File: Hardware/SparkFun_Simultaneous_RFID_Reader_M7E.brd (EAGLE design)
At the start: 35.6 x 61 mm, 76 parts, among them J5 U.FL, U1 UHF_RFID_NANO_MODULE_M7E_HECTO, U2 CH340C

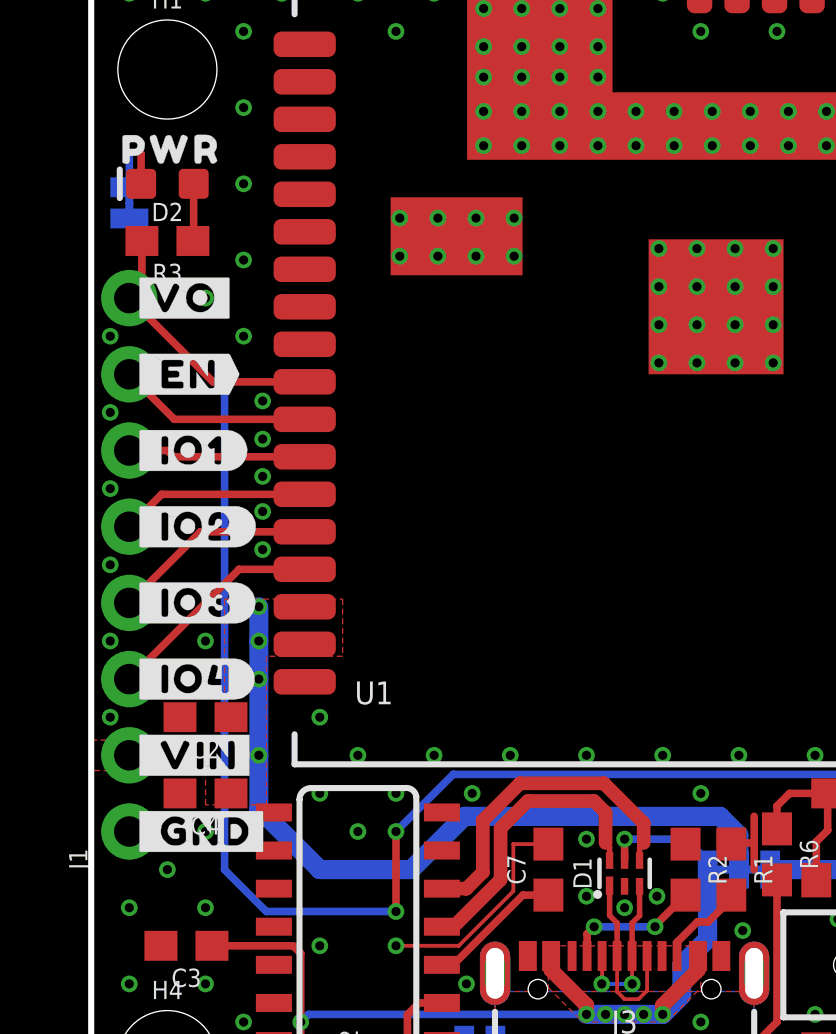
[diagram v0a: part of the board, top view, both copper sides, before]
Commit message: Design review updates
Add polygons to better fan out USB traces from ESD diode pads
Nudge R3 away from VOUT pad
Add VOUT range to schematic
Swap power LED and resistor for new version
Move via out of VO silk label
Nudge USB traces to get better GND pour around C7
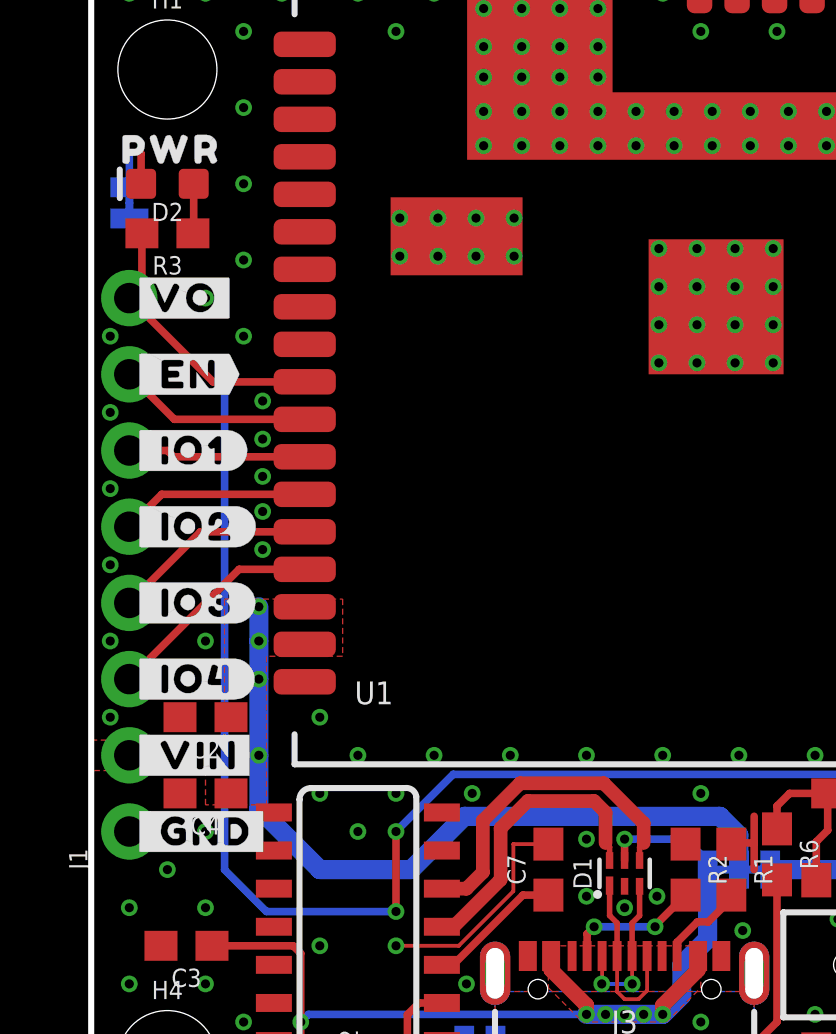
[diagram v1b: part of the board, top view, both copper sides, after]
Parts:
- moved R3 0.25 mm to (2.54, 30.1)
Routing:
- added copper zone on layer 1, net USB_N
- added copper zone on layer 1, net USB_P
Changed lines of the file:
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@@
 <drawing>
 <settings>
-<setting alwaysvectorfont="yes"/>
+<setting alwaysvectorfont="no"/>
 <setting verticaltext="up"/>
 </settings>
@@
 <attribute name="VALUE" x="0.127" y="31.115" size="0.6096" layer="28" font="vector" ratio="20" rot="MR90" align="top-center"/>
 </element>
-<element name="R3" library="SparkFun-Resistors" package="0603" value="1k" x="2.54" y="29.845" smashed="yes" rot="R180">
-<attribute name="NAME" x="2.54" y="29.083" size="0.6096" layer="25" font="vector" ratio="20" rot="R180" align="bottom-center"/>
-<attribute name="PROD_ID" value="RES-07856" x="2.54" y="29.845" size="1.778" layer="27" font="vector" ratio="15" rot="R180" display="off"/>
-<attribute name="VALUE" x="2.54" y="30.607" size="0.6096" layer="27" font="vector" ratio="20" rot="R180" align="top-center"/>
+<element name="R3" library="SparkFun-Resistors" package="0603" value="1k" x="2.54" y="30.099" smashed="yes" rot="R180">
+<attribute name="NAME" x="2.54" y="29.337" size="0.6096" layer="25" font="vector" ratio="20" rot="R180" align="bottom-center"/>
+<attribute name="PROD_ID" value="RES-07856" x="2.54" y="30.099" size="1.778" layer="27" font="vector" ratio="15" rot="R180" display="off"/>
+<attribute name="VALUE" x="2.54" y="30.861" size="0.6096" layer="27" font="vector" ratio="20" rot="R180" align="top-center"/>
 </element>
 <element name="U$49" library="output" package="#PWR#0" value="" x="1.905" y="31.115" smashed="yes" rot="MR0"/>
@@
 <wire x1="17.145" y1="10.795" x2="16.764" y2="11.176" width="0.4572" layer="1"/>
 <wire x1="16.764" y1="11.176" x2="14.5542" y2="11.176" width="0.4572" layer="1"/>
+<polygon width="0.18541875" layer="1" isolate="0.127" thermals="no">
+<vertex x="17.2974" y="9.4234"/>
+<vertex x="17.2974" y="9.906"/>
+<vertex x="17.018" y="9.906"/>
+<vertex x="17.018" y="9.7028"/>
+</polygon>
 </signal>
 <signal name="USB_N" class="1">
@@
 <wire x1="18.415" y1="10.4394" x2="17.08658125" y2="11.76781875" width="0.4572" layer="1"/>
 <wire x1="17.08658125" y1="11.76781875" x2="14.29778125" y2="11.76781875" width="0.4572" layer="1"/>
+<polygon width="0.18541875" layer="1" isolate="0.127" thermals="no">
+<vertex x="18.2626" y="9.4234"/>
+<vertex x="18.2626" y="9.906"/>
+<vertex x="18.542" y="9.906"/>
+<vertex x="18.542" y="9.7028"/>
+</polygon>
 </signal>
 <signal name="V_USB">
@@
 <contactref element="R3" pad="1"/>
 <contactref element="D2" pad="A"/>
-<wire x1="3.39" y1="29.845" x2="3.417" y2="29.872" width="0.254" layer="1"/>
-<wire x1="3.417" y1="29.872" x2="3.417" y2="31.75" width="0.254" layer="1"/>
+<wire x1="3.39" y1="30.099" x2="3.417" y2="30.126" width="0.254" layer="1"/>
+<wire x1="3.417" y1="30.126" x2="3.417" y2="31.75" width="0.254" layer="1"/>
 </signal>
 <signal name="N$6">
@@
 <wire x1="29.21" y1="10.16" x2="28.575" y2="10.795" width="0.254" layer="16"/>
 <contactref element="R3" pad="2"/>
-<wire x1="1.69" y1="28.36" x2="1.69" y2="29.845" width="0.254" layer="1"/>
+<wire x1="1.69" y1="28.36" x2="1.69" y2="30.099" width="0.254" layer="1"/>
 <wire x1="1.27" y1="27.94" x2="1.69" y2="28.36" width="0.254" layer="1"/>
 </signal>

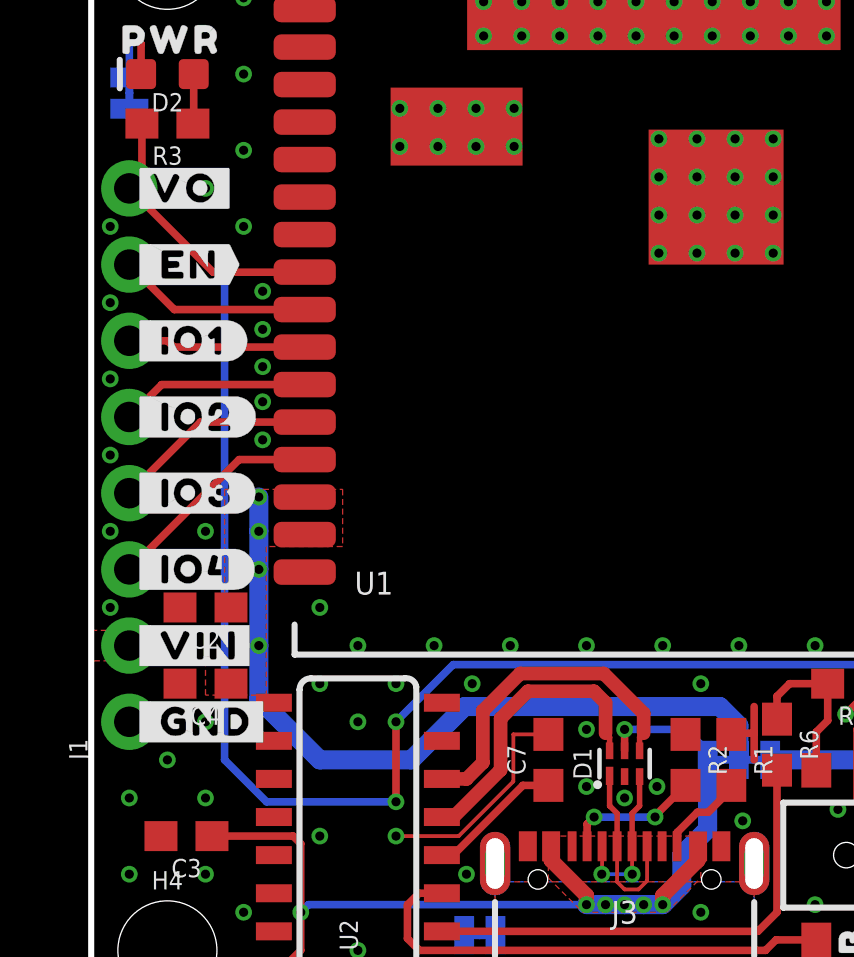
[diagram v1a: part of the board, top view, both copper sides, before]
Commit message: Design review update
Actually update the power LED and resistor this time
Actually move the via on the VO silk this time
Actually nudge USB traces to get better GND pour around C7 this time
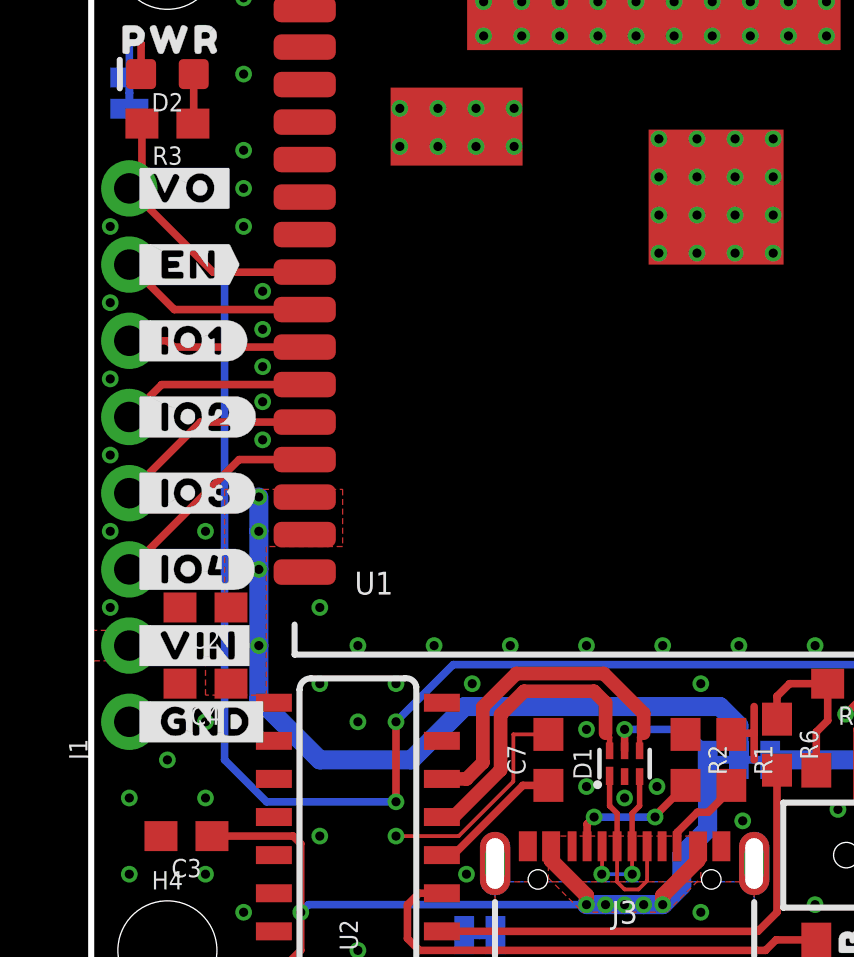
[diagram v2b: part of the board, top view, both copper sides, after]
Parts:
- R3: value 1k -> 4.7k
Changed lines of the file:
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@@
 <element name="D2" library="SparkFun-LED" package="LED-0603" value="Red" x="2.54" y="31.75" smashed="yes" rot="R180">
 <attribute name="NAME" x="2.54" y="31.115" size="0.6096" layer="25" font="vector" ratio="20" rot="R180" align="bottom-center"/>
-<attribute name="PROD_ID" value="DIO-00819" x="2.54" y="31.75" size="1.778" layer="27" font="vector" ratio="15" rot="R180" display="off"/>
+<attribute name="PROD_ID" value="DIO-17976" x="2.54" y="31.75" size="1.778" layer="27" font="vector" ratio="15" rot="R180" display="off"/>
 <attribute name="VALUE" value="Red" x="2.54" y="32.385" size="0.6096" layer="27" font="vector" ratio="20" rot="R180" align="top-center"/>
 </element>
@@
 <attribute name="VALUE" x="0.127" y="31.115" size="0.6096" layer="28" font="vector" ratio="20" rot="MR90" align="top-center"/>
 </element>
-<element name="R3" library="SparkFun-Resistors" package="0603" value="1k" x="2.54" y="30.099" smashed="yes" rot="R180">
+<element name="R3" library="SparkFun-Resistors" package="0603" value="4.7k" x="2.54" y="30.099" smashed="yes" rot="R180">
 <attribute name="NAME" x="2.54" y="29.337" size="0.6096" layer="25" font="vector" ratio="20" rot="R180" align="bottom-center"/>
-<attribute name="PROD_ID" value="RES-07856" x="2.54" y="30.099" size="1.778" layer="27" font="vector" ratio="15" rot="R180" display="off"/>
-<attribute name="VALUE" x="2.54" y="30.861" size="0.6096" layer="27" font="vector" ratio="20" rot="R180" align="top-center"/>
+<attribute name="PROD_ID" value="RES-07857" x="2.54" y="30.099" size="1.778" layer="27" font="vector" ratio="15" rot="R180" display="off"/>
+<attribute name="VALUE" value="4.7k" x="2.54" y="30.861" size="0.6096" layer="27" font="vector" ratio="20" rot="R180" align="top-center"/>
 </element>
 <element name="U$49" library="output" package="#PWR#0" value="" x="1.905" y="31.115" smashed="yes" rot="MR0"/>
@@
 <via x="5.08" y="36.83" extent="1-16" drill="0.3048"/>
 <via x="3.81" y="33.02" extent="1-16" drill="0.3048"/>
-<via x="3.81" y="27.94" extent="1-16" drill="0.3048"/>
+<via x="5.08" y="27.94" extent="1-16" drill="0.3048"/>
 <via x="5.08" y="1.27" extent="1-16" drill="0.3048"/>
 <via x="3.81" y="5.08" extent="1-16" drill="0.3048"/>
@@
 <wire x1="11.69" y1="6.985" x2="12.0766375" y2="6.985" width="0.4572" layer="1"/>
 <wire x1="12.0766375" y1="6.985" x2="13.64741875" y2="8.55578125" width="0.4572" layer="1"/>
-<wire x1="14.5542" y1="11.176" x2="13.64741875" y2="10.26921875" width="0.4572" layer="1"/>
-<wire x1="13.64741875" y1="8.55578125" x2="13.64741875" y2="10.26921875" width="0.4572" layer="1"/>
+<wire x1="14.4272" y1="11.176" x2="13.64741875" y2="10.39621875" width="0.4572" layer="1"/>
+<wire x1="13.64741875" y1="8.55578125" x2="13.64741875" y2="10.39621875" width="0.4572" layer="1"/>
 <wire x1="17.28" y1="9.193" x2="17.28" y2="9.644" width="0.18541875" layer="1"/>
 <wire x1="17.28" y1="9.644" x2="17.145" y2="9.779" width="0.18541875" layer="1"/>
 <wire x1="17.145" y1="9.779" x2="17.145" y2="10.795" width="0.4572" layer="1"/>
 <wire x1="17.145" y1="10.795" x2="16.764" y2="11.176" width="0.4572" layer="1"/>
-<wire x1="16.764" y1="11.176" x2="14.5542" y2="11.176" width="0.4572" layer="1"/>
+<wire x1="16.764" y1="11.176" x2="14.4272" y2="11.176" width="0.4572" layer="1"/>
 <polygon width="0.18541875" layer="1" isolate="0.127" thermals="no">
 <vertex x="17.2974" y="9.4234"/>
@@
 <wire x1="11.69" y1="8.255" x2="12.5084375" y2="8.255" width="0.4572" layer="1"/>
 <wire x1="12.5084375" y1="8.255" x2="13.0556" y2="8.8021625" width="0.4572" layer="1"/>
-<wire x1="13.0556" y1="8.8021625" x2="13.0556" y2="10.5256375" width="0.4572" layer="1"/>
-<wire x1="14.29778125" y1="11.76781875" x2="13.0556" y2="10.5256375" width="0.4572" layer="1"/>
+<wire x1="13.0556" y1="8.8021625" x2="13.0556" y2="10.6526375" width="0.4572" layer="1"/>
+<wire x1="14.17078125" y1="11.76781875" x2="13.0556" y2="10.6526375" width="0.4572" layer="1"/>
 <wire x1="18.28" y1="9.193" x2="18.28" y2="9.644" width="0.18541875" layer="1"/>
 <wire x1="18.28" y1="9.644" x2="18.415" y2="9.779" width="0.18541875" layer="1"/>
 <wire x1="18.415" y1="9.779" x2="18.415" y2="10.4394" width="0.4572" layer="1"/>
 <wire x1="18.415" y1="10.4394" x2="17.08658125" y2="11.76781875" width="0.4572" layer="1"/>
-<wire x1="17.08658125" y1="11.76781875" x2="14.29778125" y2="11.76781875" width="0.4572" layer="1"/>
+<wire x1="17.08658125" y1="11.76781875" x2="14.17078125" y2="11.76781875" width="0.4572" layer="1"/>
 <polygon width="0.18541875" layer="1" isolate="0.127" thermals="no">
 <vertex x="18.2626" y="9.4234"/>

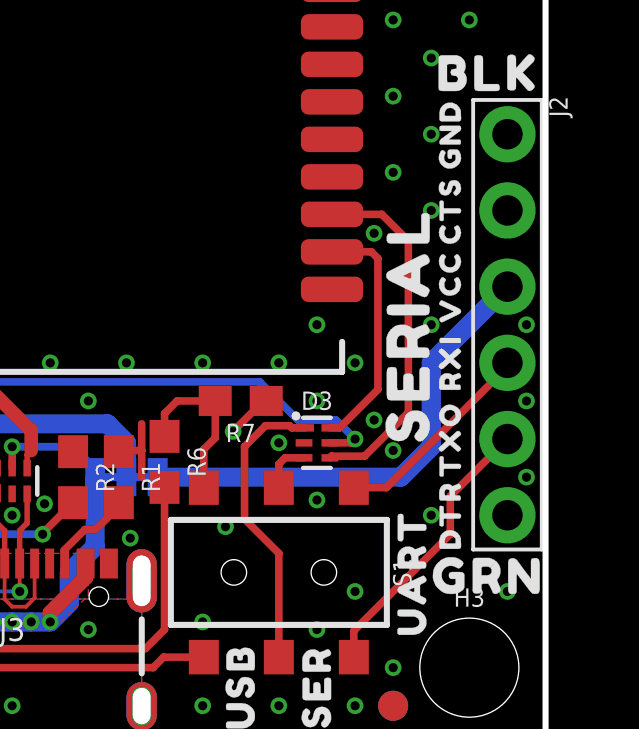
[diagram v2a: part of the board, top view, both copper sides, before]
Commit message: Design review updates
Update section titles in schematic
Remote DTR and CTS silk from serial header
Add ordering instructions
Update measures
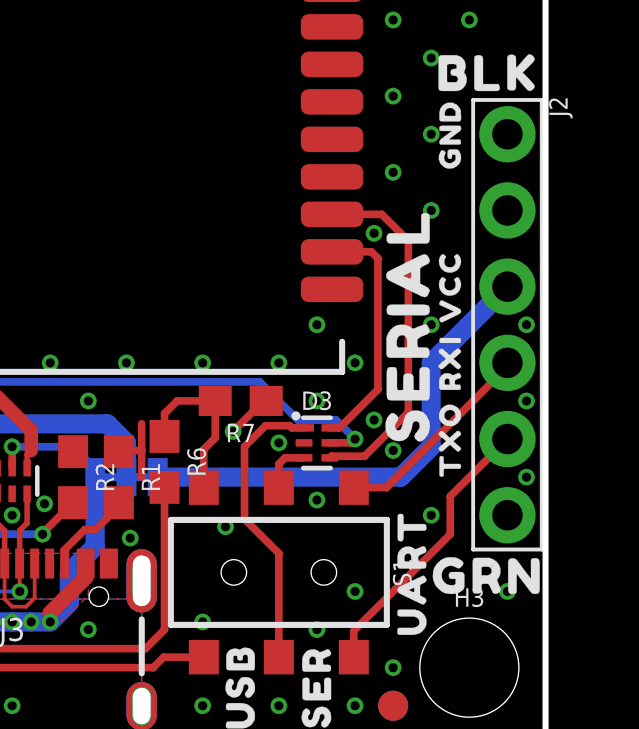
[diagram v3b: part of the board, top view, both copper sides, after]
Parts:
- added LOGO4: SPECIAL_INSTRUCTIONS-ORDERING, SparkFun-Aesthetics:ORDERING_INSTRUCTIONS
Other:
- board text added: "2-layer 1oz copper Board thickness: 1.6mm Material: TG135-140 Soldermask: Red Silkscreen: White Surface Finish: Lead-Free HASL"

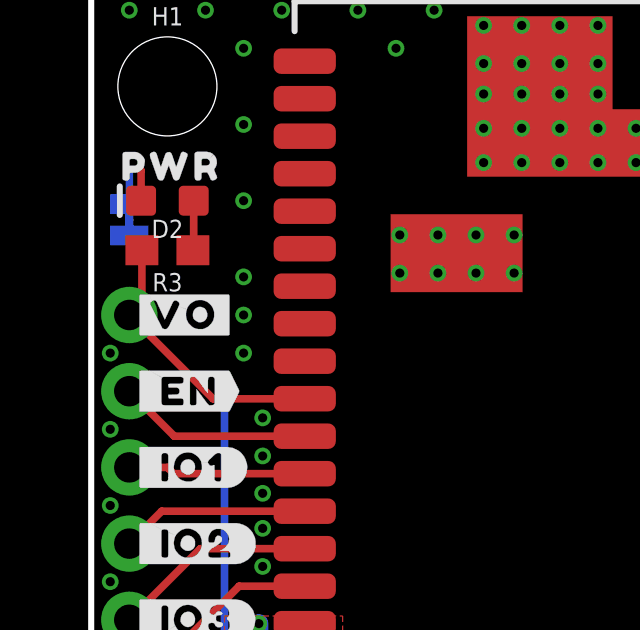
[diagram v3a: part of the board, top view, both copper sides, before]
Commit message: Fix VO silk label
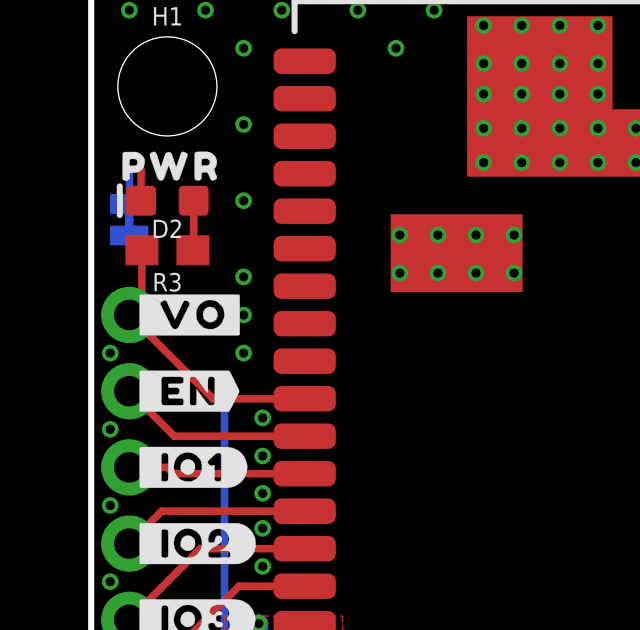
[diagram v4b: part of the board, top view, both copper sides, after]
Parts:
- removed U$9: (no value), output:#VO#1
- added U$21: (no value), output:#_VO#0
- U$18: device output:#VO#0 -> output:#VO_#0
- flipped U$18 to the bottom
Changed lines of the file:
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@@
 <drawing>
 <settings>
-<setting alwaysvectorfont="no"/>
+<setting alwaysvectorfont="yes"/>
 <setting verticaltext="up"/>
 </settings>
@@
 <element name="U$4" library="output" package="#VCC#0" value="" x="22.987" y="8.89" smashed="yes" rot="MR0"/>
 <element name="U$17" library="output" package="#VIN_SEL#0" value="" x="21.59" y="7.239" smashed="yes" rot="MR0"/>
-<element name="U$18" library="output" package="#VO#0" value="" x="1.27" y="27.94" smashed="yes"/>
-<element name="U$9" library="output" package="#VO#1" value="" x="1.27" y="27.94" smashed="yes" rot="MR0"/>
 <element name="R6" library="SparkFun-Resistors" package="0603" value="5.1k" x="22.86" y="9.398" smashed="yes" rot="R270">
 <attribute name="NAME" x="23.622" y="9.398" size="0.6096" layer="25" font="vector" ratio="20" rot="R270" align="bottom-center"/>
@@
 </element>
 <element name="LOGO4" library="SparkFun-Aesthetics" package="ORDERING_INSTRUCTIONS" value="SPECIAL_INSTRUCTIONS-ORDERING" x="46.99" y="50.8" smashed="yes"/>
+<element name="U$21" library="output" package="#_VO#0" value="" x="1.27" y="27.94" smashed="yes"/>
+<element name="U$18" library="output" package="#VO_#0" value="" x="1.27" y="27.94" smashed="yes" rot="MR0"/>
 </elements>
 <signals>
